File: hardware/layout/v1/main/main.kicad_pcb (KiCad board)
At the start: 4 copper layers, 32 x 52 mm, 47 parts, among them J1 12-32V + RS485, J2 Crown board, J3 Probe board, J4 PMSA003I PM, J5 Power board, Q1 AO3400A, SW1 SERVICE, U2 LM66100, U3 XIAO ESP32C6, U4 ADS1115IDGSR, U5 LSM6DS3TR-C, U7 SP3485EN-L/TR

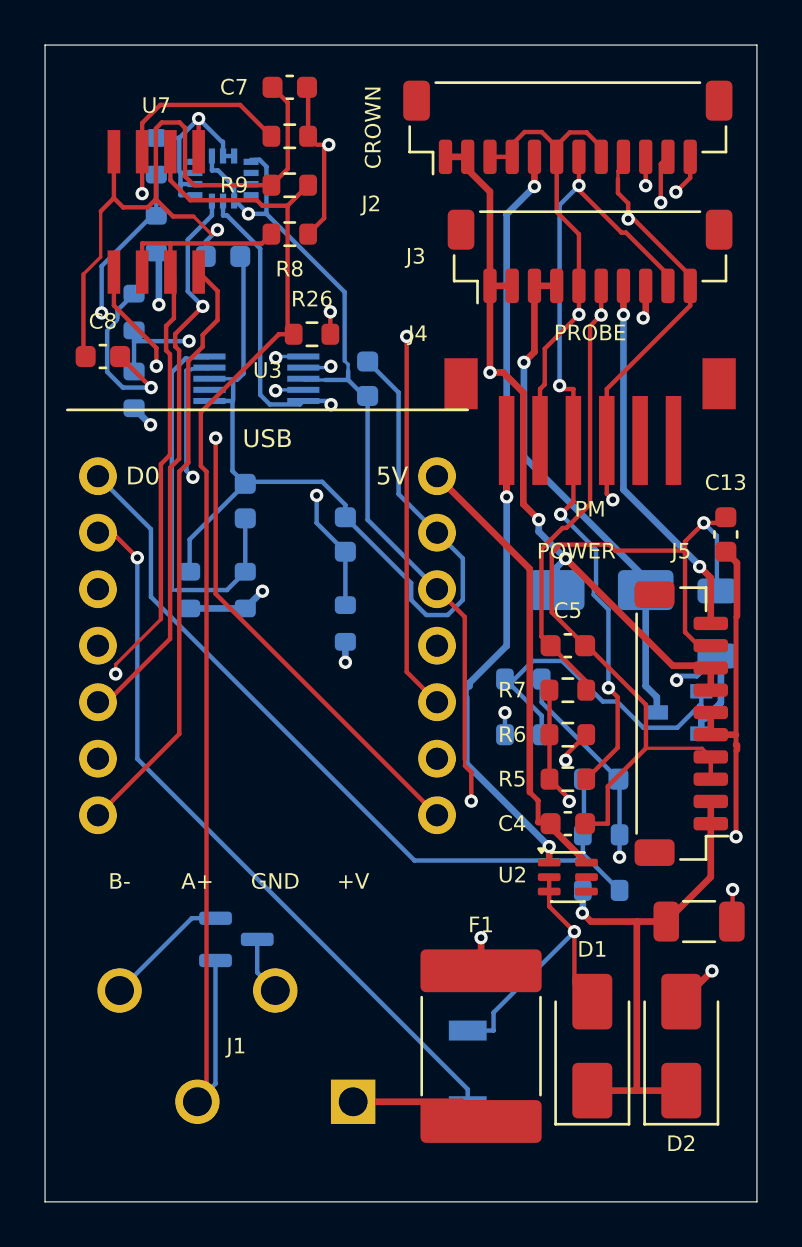
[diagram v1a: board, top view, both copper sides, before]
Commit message: Update AGENTS.md, CALIBRATION.md, and README.md for PTFE dome diffuser, probe heater setpoint change to −7.6 °C, crown preamp bias mode, RS-485 fail-safe bias note, and enclosure seal test
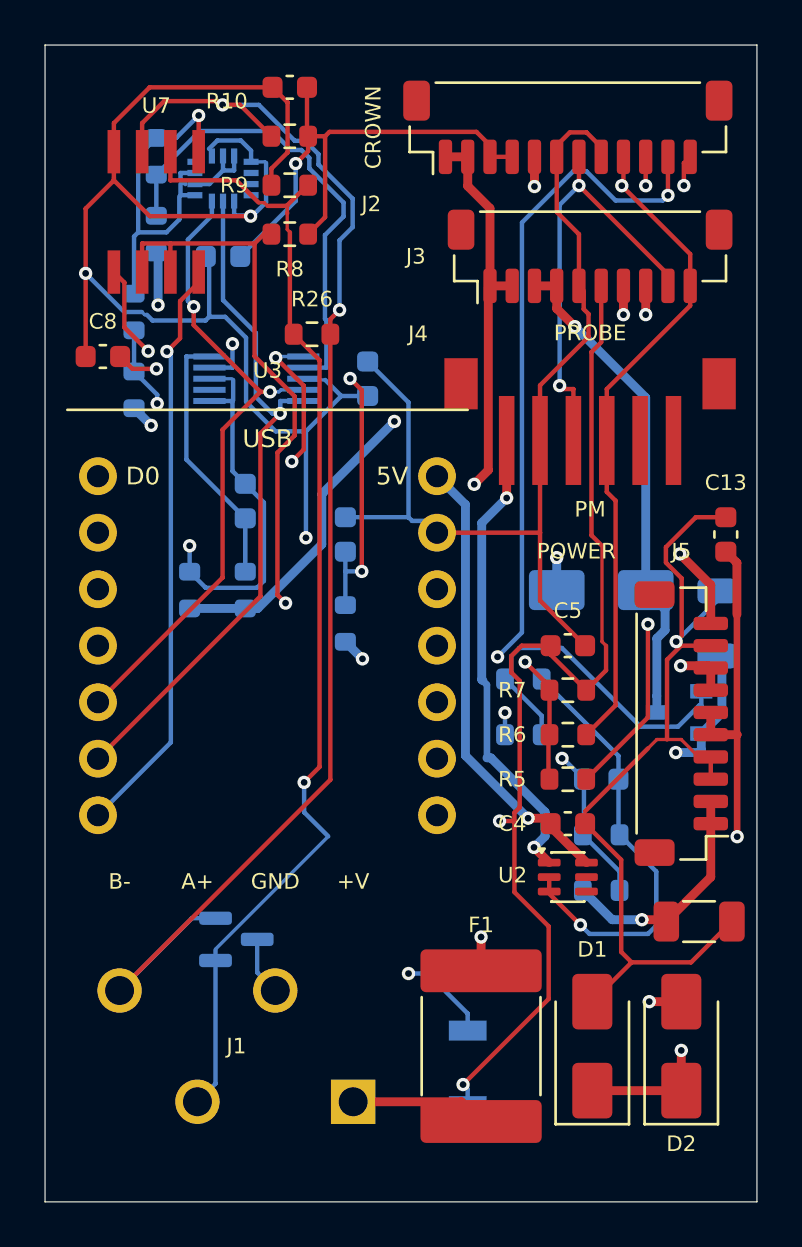
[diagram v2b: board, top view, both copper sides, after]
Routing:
- net GND: track 150.8 -> 169.1 mm, vias 8 -> 7
- net HEAT_PWM: track 21.1 -> 33.1 mm
- net CROWN_IRQ: track 31.9 -> 40.9 mm, vias 2 -> 1
- net I2C_SCL: track 89.0 -> 80.5 mm, vias 4 -> 2
- net NTC_SENSE: track 80.1 -> 71.6 mm
- net RS485_DE: track 43.9 -> 35.8 mm
- net MON_5V: track 9.79 -> 17.5 mm, vias 2 -> 3
- net CROWN_BOOT0: track 36.5 -> 43.6 mm
- net MON_PROBE: track 17.8 -> 11.8 mm
- net RS485_B: track 67.5 -> 61.6 mm
- net +5V: track 82.3 -> 88.1 mm
- net RS485_A: track 57.7 -> 52.4 mm, vias 0 -> 1
- net VIN_FUSED: track 14.4 -> 11.7 mm
- net MON_REFL: track 17.4 -> 20.1 mm, vias 2 -> 3
- net CROWN_NRST: track 30.2 -> 32.8 mm, vias 1 -> 2
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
